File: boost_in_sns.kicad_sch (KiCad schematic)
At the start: 0 parts

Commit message: Working on power board
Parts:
- added C17: 100nF, Capacitor_SMD:C_1206_3216Metric, symbol Device:C
- added U2: PINA745AIRELR, REL0014A_PINA745AIRELR_TEX, symbol _INA745:PINA745AIRELR
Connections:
- new net: U2.1 (SH+), U2.2 (IN+)
- new net: U2.8 (SH-), U2.9 (IN-)
- new net +5V: C17.1, U2.11 (VS)
- new net GND: C17.2, U2.12 (GND), U2.3 (A1), U2.4 (A0)
- new net I2C.SCL: U2.6 (SCL)
- new net I2C.SDA: U2.5 (SDA)
- new net PANEL_DRV: U2.7 (IS-)
- new net PANEL_IN: U2.13 (VBUS), U2.14 (IS+)
- new net PANEL_IN_ALERT: U2.10 (ALERT)

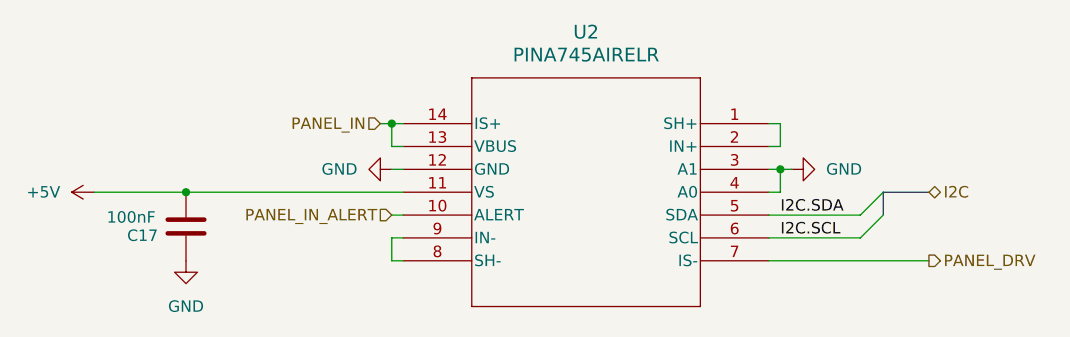
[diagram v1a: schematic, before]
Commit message: Adding more schematic blocks
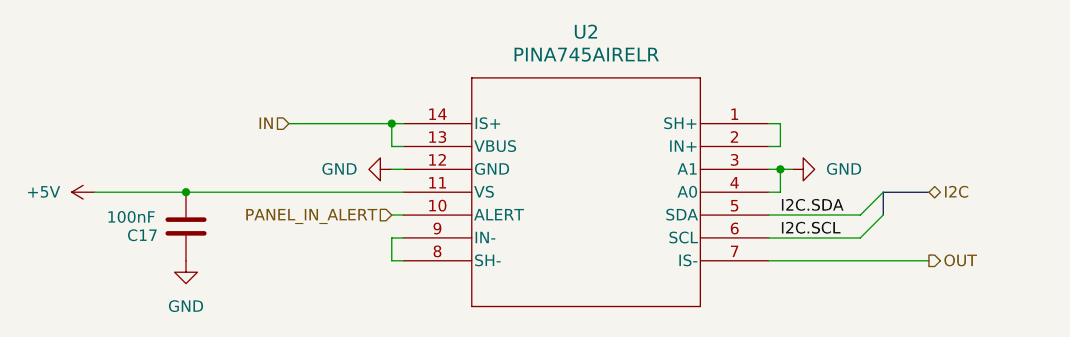
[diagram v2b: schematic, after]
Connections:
- net PANEL_DRV renamed OUT
- net PANEL_IN renamed IN
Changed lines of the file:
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@@
 	(wire
 		(pts
-			(xy 119.38 64.77) (xy 120.65 64.77)
+			(xy 109.22 64.77) (xy 120.65 64.77)
 		)
 		(stroke
@@
 		)
 	)
-	(hierarchical_label "PANEL_IN"
+	(hierarchical_label "IN"
 		(shape input)
-		(at 119.38 64.77 180)
+		(at 109.22 64.77 180)
 		(effects
 			(font
@@
 		)
 	)
-	(hierarchical_label "PANEL_DRV"
+	(hierarchical_label "OUT"
 		(shape output)
 		(at 180.34 80.01 0)
